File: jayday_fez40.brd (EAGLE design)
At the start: 50 x 48 mm, 52 parts, among them IC1 GHI_STM32F40X, IC2 LM1117MP-3.3, IC9 MIC4680-ADJ, Q2 32.768Khz, U3 MICROSD_MICROSD, X4 DX2R005HN2E700

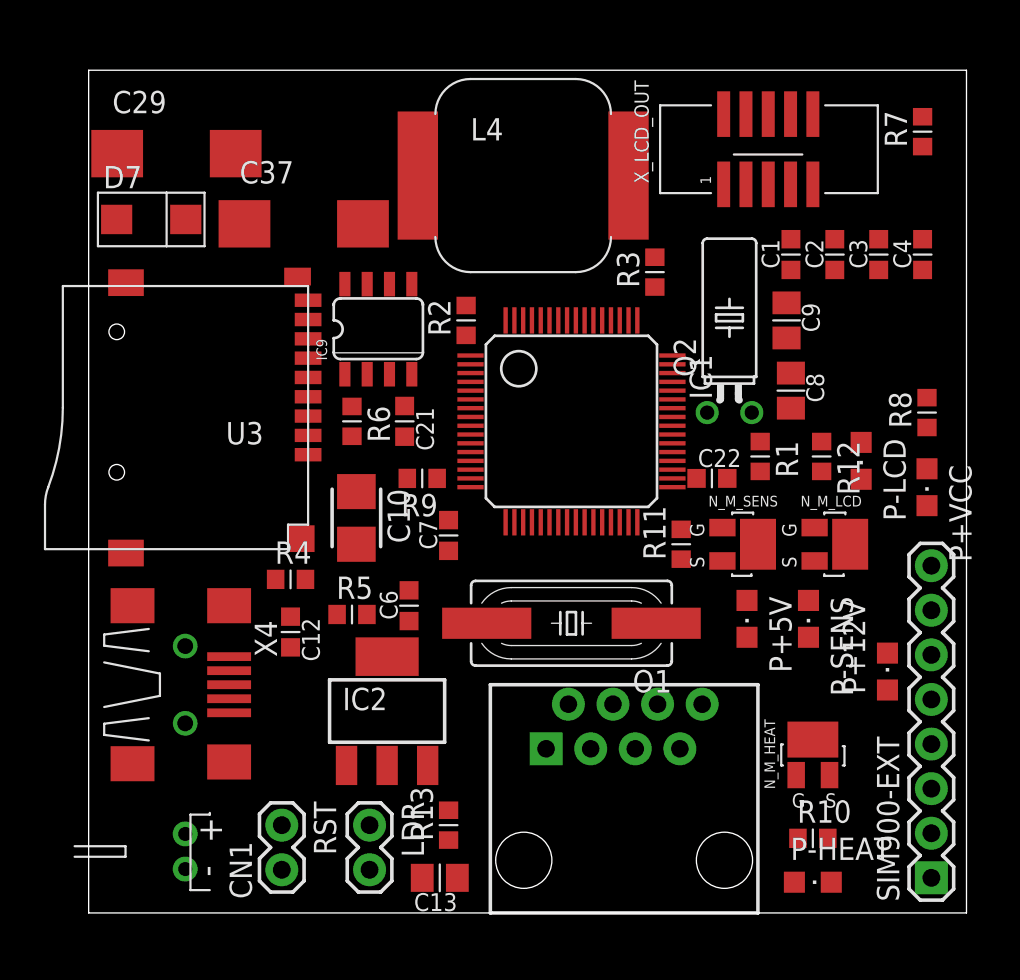
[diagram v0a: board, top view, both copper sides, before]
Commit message: layed out board.. 2 traces left
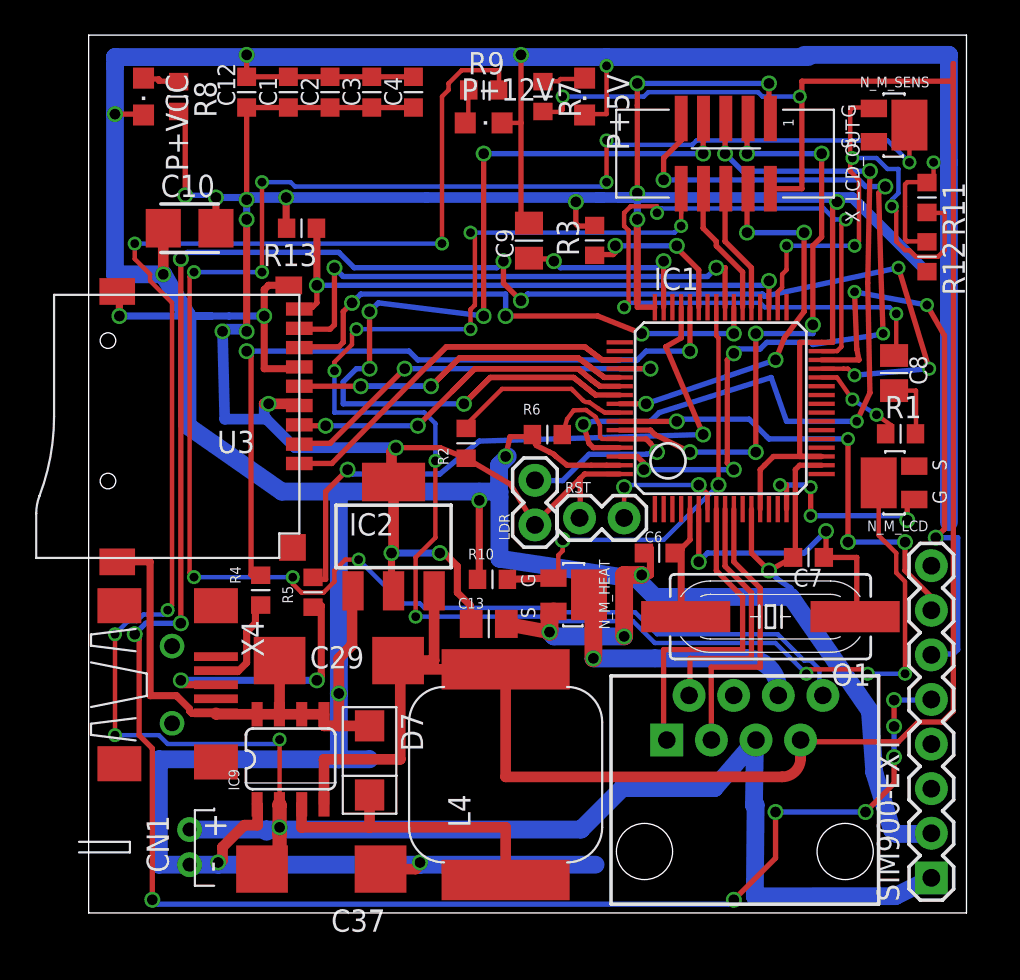
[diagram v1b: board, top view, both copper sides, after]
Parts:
- removed C21, C22: 18pF, rcl:C0603K
- removed P-HEAT, P-LCD, P-SENS: (no value), led:CHIPLED_0805
- removed Q2: 32.768Khz, crystal:TC38H
- R10, R11, R12: value 330 -> 100K
- moved P+VCC 49.9 mm to (3.12, 46.5)
- moved R8 46.3 mm to (5.12, 46.5), turned to 270 degrees
- moved P+12V 38.8 mm to (22.5, 45.0), turned to 270 degrees
- moved C37 36.8 mm to (13.2, 2.50), turned to 180 degrees
- moved R13 35.0 mm to (12.1, 39.0), turned to 180 degrees
- moved L4 34.1 mm to (23.8, 7.88), turned to 90 degrees
- moved D7 33.2 mm to (16.0, 8.75), turned to 270 degrees
- moved P+5V 31.2 mm to (28.2, 46.5)
- moved C12 30.9 mm to (9.00, 46.8), turned to 90 degrees
- moved C4 30.4 mm to (18.5, 46.8)
- moved C29 30.3 mm to (14.2, 14.4)
- moved C3 30.3 mm to (16.1, 46.8)
- moved C2 30.2 mm to (13.8, 46.8)
- moved C1 30.1 mm to (11.4, 46.8)
- moved RST 26.2 mm to (30.5, 22.5), turned to 180 degrees
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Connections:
- removed net N$14: P-HEAT.A, R10.1
- removed net N$15: P-SENS.A, R11.1
- removed net N$16: P-LCD.A, R12.1
- net GND: now also R10.1, R11.1, R12.1; no longer C21.2, C22.2, P-HEAT.C, P-LCD.C, P-SENS.C
- net PC14/XO32: no longer C21.1, Q2.2
- net PC15/XI32: no longer C22.1, Q2.1
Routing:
- net GND: track 0.00 -> 367.1 mm, vias 0 -> 17
- net VCC: track 0.00 -> 183.5 mm, vias 0 -> 17
- net PB10/I2C2_SCL/SPI2_SCK/UART3_TX: track 0.00 -> 148.7 mm, vias 0 -> 15
- net +12V: track 0.00 -> 134.3 mm, vias 0 -> 7
- net +5V: track 0.00 -> 132.8 mm, vias 0 -> 2
- net SENS_OUT: track 0.00 -> 110.5 mm, vias 0 -> 9
- net LCD_OUT: track 0.00 -> 90.3 mm, vias 0 -> 10
- net PB3/J_TDO/PWM/SPI1_SCK: track 0.00 -> 62.0 mm, vias 0 -> 6
- net PB9/I2C1_SDA/CAN1_TX: track 0.00 -> 48.1 mm, vias 0 -> 6
- net N$3: track 0.00 -> 46.0 mm, vias 0 -> 4
- net PB8/I2C1_SCL/CAN1_RX: track 0.00 -> 46.0 mm, vias 0 -> 4
- net N$5: track 0.00 -> 41.6 mm, vias 0 -> 2
- net N$7: track 0.00 -> 36.7 mm, vias 0 -> 2
- net PB7/I2C1_SDA/UART1_RX: track 0.00 -> 34.9 mm, vias 0 -> 6
- net PC12/SD_CLK: track 0.00 -> 34.5 mm, vias 0 -> 2
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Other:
- board size 50 x 48 mm -> 50 x 50 mm

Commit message: finished layout
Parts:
- removed N_M_SENS: SI2312BDS, ozlollc:TO-236
- removed P+12V, P+5V: (no value), led:CHIPLED_0805
- removed X_LCD_OUT: SHF105, ozlollc:GAD_PAC_SMD
- added +12V, +5V: (no value), led:CHIPLED_0805
- added LCD_OUT: SHF105, ozlollc:GAD_PAC_SMD
- added M_SENS: SI2312BDS, ozlollc:TO-236
- moved R9 22.6 mm to (45.1, 47.8), turned to 270 degrees
- moved R7 19.5 mm to (45.2, 44.1)
- moved R11 8.11 mm to (40.4, 37.4), turned to 0 degrees
- moved R3 8.00 mm to (21.8, 42.2)
- moved C9 7.53 mm to (18.7, 42.3)
- moved IC1 5.76 mm to (30.8, 31.1)
- moved R1 5.18 mm to (43.1, 31.4)
- moved C8 4.65 mm to (43.1, 34.5), turned to 0 degrees
- moved R12 3.73 mm to (46.9, 33.8)
- moved R6 2.64 mm to (24.2, 25.5)
- moved LDR 2.28 mm to (25.0, 22.4), turned to 180 degrees
- moved C7 1.88 mm to (42.9, 20.2)
- moved C6 0.90 mm to (33.2, 20.0)
- turned N_M_LCD to 270 degrees
- renumbered P+VCC to VCC
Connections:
- net +5V: now also LCD_OUT.2; no longer X_LCD_OUT.2
- net GND: now also +12V.C, +5V.C, M_SENS.2; no longer N_M_SENS.2, P+12V.C, P+5V.C
- net LCD_OUT: now also LCD_OUT.10; no longer X_LCD_OUT.10
- net N$11: now also +5V.A; no longer P+5V.A
- net N$13: now also +12V.A; no longer P+12V.A
- net PB13/SPI2_SCK/CAN2_TX: now also M_SENS.1; no longer N_M_SENS.1
- net PB3/J_TDO/PWM/SPI1_SCK: now also LCD_OUT.7; no longer X_LCD_OUT.7
- net PB4/J_TRST/PWM/SPI1_MISO: now also LCD_OUT.4; no longer X_LCD_OUT.4
- net PB7/I2C1_SDA/UART1_RX: now also LCD_OUT.3; no longer X_LCD_OUT.3
- net PB8/I2C1_SCL/CAN1_RX: now also LCD_OUT.5; no longer X_LCD_OUT.5
- net PB9/I2C1_SDA/CAN1_TX: now also LCD_OUT.9; no longer X_LCD_OUT.9
- net PC6/UART6_TX: now also LCD_OUT.6; no longer X_LCD_OUT.6
- net PC7/UART6_RX: now also LCD_OUT.8; no longer X_LCD_OUT.8
- net SENS_OUT: now also M_SENS.3; no longer N_M_SENS.3
- net VCC: now also LCD_OUT.1; no longer X_LCD_OUT.1
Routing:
- net PB10/I2C2_SCL/SPI2_SCK/UART3_TX: track 148.7 -> 33.9 mm, vias 15 -> 0
- net SENS_OUT: track 110.5 -> 33.0 mm, vias 9 -> 0
- net GND: track 367.1 -> 428.6 mm, vias 17 -> 10
- net +5V: track 132.8 -> 189.4 mm
- net LCD_OUT: track 90.3 -> 46.6 mm, vias 10 -> 2
- net N$3: track 46.0 -> 5.82 mm, vias 4 -> 2
- net PB3/J_TDO/PWM/SPI1_SCK: track 62.0 -> 23.1 mm, vias 6 -> 0
- net +12V: track 134.3 -> 172.8 mm, vias 7 -> 2
- net PC12/SD_CLK: track 34.5 -> 15.2 mm
- net PB6/I2C1_SCL/UART1_TX: track 27.1 -> 42.7 mm, vias 4 -> 2
- net PB13/SPI2_SCK/CAN2_TX: track 30.9 -> 15.6 mm, vias 4 -> 2
- net VCC: track 183.5 -> 198.2 mm, vias 17 -> 6
- net PB9/I2C1_SDA/CAN1_TX: track 48.1 -> 60.6 mm, vias 6 -> 2
- net PB11/I2C2_SDA/UART3_RX: track 33.2 -> 45.6 mm, vias 3 -> 0
- net PB8/I2C1_SCL/CAN1_RX: track 46.0 -> 33.6 mm, vias 4 -> 2
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- added copper zone on layer 1, net GND
- added copper zone on layer 16, net GND
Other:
- board text added: "(c) ozlo, llc - 2012 - rev 1.0"
- board text added: "Based on GHI's OSHW FEZ Cerberus"

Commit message: added bom, and shipped pcb
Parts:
- moved C6 0.50 mm to (33.6, 20.4)
- moved R9 0.23 mm to (45.3, 47.8)
- moved +5V 0.10 mm to (47.7, 44.1)
- moved R7 0.09 mm to (45.3, 44.1)
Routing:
- net +12V: track 172.8 -> 170.4 mm
- net XTAL3: track 12.2 -> 13.3 mm
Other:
- board text added: "ORDER#: 62385"

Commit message: fixed R9 to 825ohms
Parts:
- R9: value 330 -> 825
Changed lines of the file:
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@@
 <setting verticaltext="up"/>
 </settings>
-<grid distance="1" unitdist="mil" unit="mil" style="lines" multiple="1" display="yes" altdistance="0.025" altunitdist="inch" altunit="inch"/>
+<grid distance="7" unitdist="mil" unit="mil" style="lines" multiple="1" display="yes" altdistance="0.025" altunitdist="inch" altunit="inch"/>
 <layers>
 <layer number="1" name="Top" color="4" fill="1" visible="yes" active="yes"/>
@@
 <attribute name="VALUE" x="45.1104" y="48.9204" size="1.27" layer="27" rot="R270"/>
 </element>
-<element name="R9" library="rcl" package="R0603" value="330" x="45.339" y="47.8282" smashed="yes" rot="R270">
+<element name="R9" library="rcl" package="R0603" value="825" x="45.339" y="47.8282" smashed="yes" rot="R270">
 <attribute name="NAME" x="43.2054" y="48.7172" size="0.8128" layer="25" rot="R270"/>
 <attribute name="VALUE" x="43.307" y="48.7172" size="1.27" layer="27" rot="R270"/>
